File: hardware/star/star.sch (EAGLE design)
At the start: 153 parts, among them IC1 MAX481CSA, IC2 LD117AS12TR, IC22 LD117AS12TR, IC3 74HCT08D, IC4 7404D, IC8 MAX481CSA, K1 T90-12VDC-TL-A, K2 T90-12VDC-TL-A, K5 AQG22110, K6 AQG22110, P1 B3B-PH-K, Q1 35A/25V/8.5mΩ, Q2 35A/25V/8.5mΩ, Q3 35A/25V/8.5mΩ, Q4 35A/25V/8.5mΩ, T1 T_PNP_MMBT5401_CHANGJ_SOT23-B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, T2 T_PNP_MMBT5401_CHANGJ_SOT23-B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, T3 T_PNP_MMBT5401_CHANGJ_SOT23-B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, T4 T_PNP_MMBT5401_CHANGJ_SOT23-B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, U1 TCLT1600, X1 MKDSN1,5/2-5,08, X2 MKDSN1,5/2-5,08, X3 MKDSN1,5/5-5,08

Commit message: I think it's good?
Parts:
- removed FIRE: MKDSN1,5/8-5,08, con-phoenix-508-jm:MKDSN1,5/8-5,08
- removed P1: B3B-PH-K, con-jst-ph:B3B-PH-K
- removed TVS1, TVS2, TVS3, TVS4: (no value), diode:DIODE-DO214AA
- removed X1, X2: MKDSN1,5/2-5,08, con-phoenix-508-jm:MKDSN1,5/2-5,08
- removed X3: MKDSN1,5/5-5,08, con-phoenix-508-jm:MKDSN1,5/5-5,08
- added 12VAC_IN, 5V/2_IN: MKDSN1,5/2-5,08, con-phoenix-508-jm:MKDSN1,5/2-5,08
- added D10, D11, D139, D20, D21, D5: SMBJ8.0CA, SMBJ8.0CA:SMBJ8.0CA
- added D22, D23, D24, D25, D26, D27, D28, D29, D30, D31: D_B5819W-SL_CHANGJ_SOD123, JLC PCB Basic Parts_loc:D_B5819W-SL_CHANGJ_SOD123
- added DMX_OUT, OVERRIDE_EN: B3B-PH-K, con-jst-ph:B3B-PH-K
- added FIRE_OUT: MKDSN1,5/8-5,08, con-phoenix-508-jm:MKDSN1,5/8-5,08
- added FOG_IN: MKDSN1,5/5-5,08, con-phoenix-508-jm:MKDSN1,5/5-5,08
- added K3: T90-12VDC-TL-A, relay:JT1A-PCB-DC12V
- added OVERRIDE_EN2: (no value), pinhead:PINHD-1X3
- added R50: R_1K_0603, JLC PCB Basic Parts_loc:R_1K_0603
- added R6: R_100K_0603, JLC PCB Basic Parts_loc:R_100K_0603
- D4: value (none) -> SMBJ8.0CA; device diode:DIODE-DO214AA -> SMBJ8.0CA:SMBJ8.0CA; DESCRIPTION (none) -> 600 Watt TVS 5.0v working, 9v clamp; LCSC_PART C80339 -> C78757
- LED_ARRAY: value (none) -> B4B-PH-K; device pinhead:PINHD-1X4 -> con-jst-ph:B4B-PH-K
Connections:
- new net N$53: FIRE_OUT-1.KL, K3G$2.P
- new net N$58: OVERRIDE_EN.1, OVERRIDE_EN2.1, R50.2
- net +14V: now also FIRE_OUT-3.KL; no longer FIRE-3.KL
- net +3V3: now also D22.C, D24.C, D26.C, D28.C, D30.C, R50.1
- net +5V: now also D15.C, D16.A, K3G$1.1
- net +5V/2: now also 5V/2_IN-2.KL, K3G$2.S; no longer D15.C, D16.A, FIRE-1.KL, X2-2.KL
- net 120_LINE: now also 12VAC_IN-1.KL; no longer X1-1.KL
- net 120_NEUTRAL: now also 12VAC_IN-2.KL, FIRE_OUT-6.KL, FIRE_OUT-8.KL, FOG_IN-5.KL; no longer FIRE-6.KL, FIRE-8.KL, X1-2.KL, X3-5.KL
- net 18: now also D21.2
- net 19: now also D4.2
- net BOOMER_BLOWER: now also D10.2
- net BOOMER_FUEL: now also D5.2
- net BOOMER_IGNITER: now also D11.2
- net GND: now also D10.1, D11.1, D139.1, D20.1, D21.1, D23.A, D25.A, D27.A, D29.A, D31.A, D4.1, D5.1, DMX_OUT.1, OVERRIDE_EN.3, OVERRIDE_EN2.3, Q4.S, R6.1; no longer D4.A, P1.1, TVS1.A, TVS2.A, TVS3.A, TVS4.A, X2-1.KL
- net GND3: now also 5V/2_IN-1.KL, FIRE_OUT-2.KL; no longer Q4.S
- net N$13: now also FOG_IN-2.KL; no longer X3-2.KL
- net N$14: now also FOG_IN-4.KL; no longer X3-4.KL
- net N$15: now also FOG_IN-1.KL; no longer X3-1.KL
- net N$17: now also D22.A, D23.C; no longer TVS1.C
- net N$22: now also OVERRIDE_EN.2, OVERRIDE_EN2.2
- net N$23: now also D30.A, D31.C, R6.2; no longer D4.C
- net N$25: now also D28.A, D29.C; no longer TVS4.C
- net N$31: now also D24.A, D25.C; no longer TVS2.C
- net N$37: now also D26.A, D27.C; no longer TVS3.C
- net N$48: now also FIRE_OUT-7.KL; no longer FIRE-7.KL
- net N$5: now also DMX_OUT.2; no longer P1.2
- net N$50: now also FIRE_OUT-5.KL; no longer FIRE-5.KL
- net N$51: now also FIRE_OUT-4.KL; no longer FIRE-4.KL
- net N$52: now also K3G$1.2; no longer FIRE-2.KL
- net N$6: now also DMX_OUT.3; no longer P1.3
- net N$7: now also FOG_IN-3.KL; no longer X3-3.KL
- net POOFER: now also D139.2
- net STAR_ENABLE: now also D20.2
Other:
- note removed: "Todo: Drive Q4 with +5 and GND Add Relay to switch +5/2 and GND3"
- moved on the sheet: 5V_CTRL_LAZERS, C1, C10, C11, C12, C13, C14, C15, C16, C17, C18, C19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

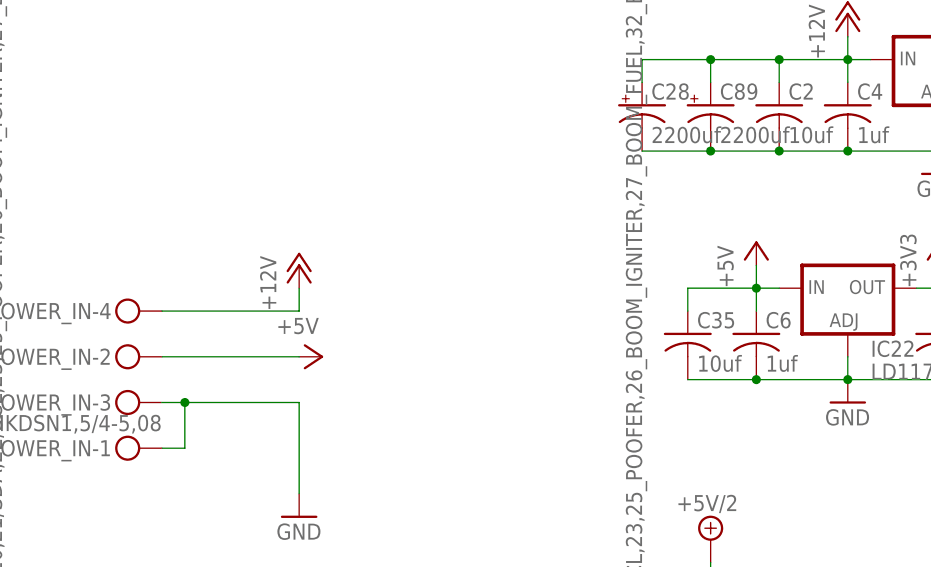
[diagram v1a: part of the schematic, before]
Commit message: Manual Routing Complete for v2
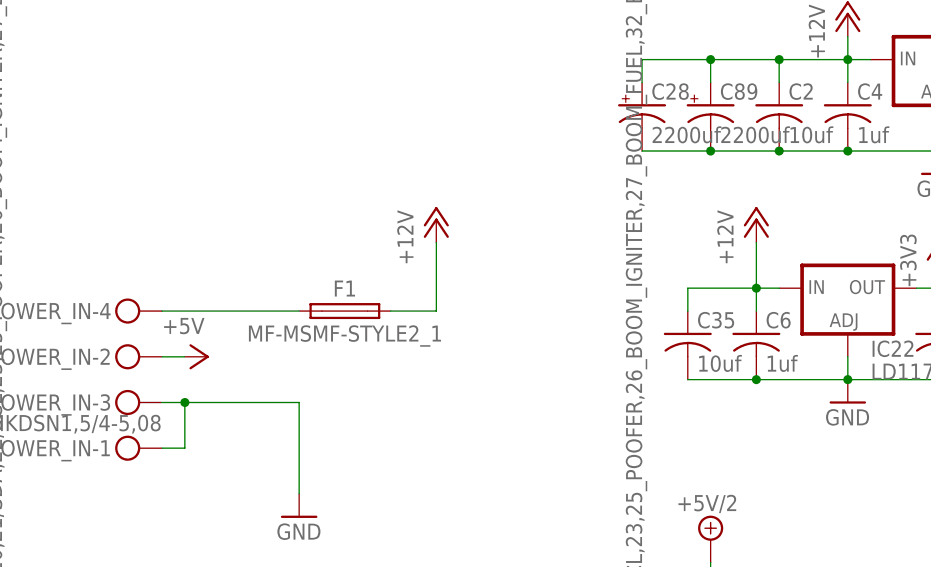
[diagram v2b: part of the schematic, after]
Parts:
- added F1: MF-MSMF-STYLE2_1, Fuse:MF-MSMF-STYLE2_1
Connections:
- new net N$59: F1.1, POWER_IN-4.KL
- net +12V: now also C35.1, C6.1, F1.2, IC22.IN; no longer POWER_IN-4.KL
- net +5V: no longer C35.1, C6.1, IC22.IN
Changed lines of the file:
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@@
 <attribute name="PRICE" value="0.5"/>
 </part>
-<part name="P+13" library="supply1" library_urn="urn:adsk.eagle:library:371" deviceset="+5V" device=""/>
 <part name="GND101" library="supply1" library_urn="urn:adsk.eagle:library:371" deviceset="GND" device=""/>
 <part name="C6" library="rcl" library_urn="urn:adsk.eagle:library:334" deviceset="C-US" device="C0805" package3d_urn="urn:adsk.eagle:package:23617/2" value="1uf">
@@
 <part name="+3V13" library="supply1" library_urn="urn:adsk.eagle:library:371" deviceset="+3V3" device=""/>
 <part name="OVERRIDE_EN2" library="pinhead" library_urn="urn:adsk.eagle:library:325" deviceset="PINHD-1X3" device="" package3d_urn="urn:adsk.eagle:package:22458/2"/>
+<part name="F1" library="Fuse" library_urn="urn:adsk.eagle:library:24934274" deviceset="MF-MSMF" device="-STYLE2_1" package3d_urn="urn:adsk.eagle:package:24934283/1">
+<attribute name="LCSC_PART" value="C78695"/>
+</part>
+<part name="P+10" library="supply1" library_urn="urn:adsk.eagle:library:371" deviceset="+12V" device=""/>
 </parts>
 <sheets>
@@
 <attribute name="VALUE" x="189.992" y="406.4762" size="1.778" layer="96"/>
 </instance>
-<instance part="P+5" gate="1" x="299.72" y="434.34" smashed="yes">
-<attribute name="VALUE" x="297.18" y="429.26" size="1.778" layer="96" rot="R90"/>
+<instance part="P+5" gate="1" x="314.96" y="439.42" smashed="yes">
+<attribute name="VALUE" x="312.42" y="434.34" size="1.778" layer="96" rot="R90"/>
 </instance>
-<instance part="P+6" gate="1" x="302.26" y="424.18" smashed="yes" rot="R270">
-<attribute name="VALUE" x="297.18" y="426.72" size="1.778" layer="96"/>
+<instance part="P+6" gate="1" x="289.56" y="424.18" smashed="yes" rot="R270">
+<attribute name="VALUE" x="284.48" y="426.72" size="1.778" layer="96"/>
 </instance>
 <instance part="GND10" gate="1" x="299.72" y="406.4" smashed="yes">
@@
 <attribute name="LCSC_PART" x="360.68" y="431.8" size="1.778" layer="96" display="off"/>
 </instance>
-<instance part="P+13" gate="1" x="350.52" y="436.88" smashed="yes">
-<attribute name="VALUE" x="347.98" y="431.8" size="1.778" layer="96" rot="R90"/>
-</instance>
 <instance part="GND101" gate="1" x="360.68" y="419.1" smashed="yes">
 <attribute name="VALUE" x="358.14" y="416.56" size="1.778" layer="96"/>
@@
 <attribute name="VALUE" x="379.73" y="259.08" size="1.778" layer="96"/>
 </instance>
+<instance part="F1" gate="G$1" x="304.8" y="429.26" smashed="yes">
+<attribute name="NAME" x="304.8" y="431.76" size="1.778" layer="95" align="center"/>
+<attribute name="VALUE" x="304.8" y="426.76" size="1.778" layer="96" align="center"/>
+<attribute name="LCSC_PART" x="304.8" y="429.26" size="1.778" layer="96" display="off"/>
+</instance>
+<instance part="P+10" gate="1" x="350.52" y="439.42" smashed="yes">
+<attribute name="VALUE" x="347.98" y="434.34" size="1.778" layer="96" rot="R90"/>
+</instance>
 </instances>
 <busses>
@@
 <net name="+12V" class="2">
 <segment>
-<pinref part="P+5" gate="1" pin="+12V"/>
-<wire x1="299.72" y1="431.8" x2="299.72" y2="429.26" width="0.1524" layer="91"/>
-<wire x1="299.72" y1="429.26" x2="284.48" y2="429.26" width="0.1524" layer="91"/>
-<pinref part="POWER_IN" gate="-4" pin="KL"/>
-</segment>
-<segment>
 <pinref part="P+12" gate="1" pin="+12V"/>
 <wire x1="302.26" y1="172.72" x2="302.26" y2="190.5" width="0.1524" layer="91"/>
@@
 <junction x="378.46" y="396.24"/>
 </segment>
+<segment>
+<pinref part="F1" gate="G$1" pin="2"/>
+<pinref part="P+5" gate="1" pin="+12V"/>
+<wire x1="309.88" y1="429.26" x2="314.96" y2="429.26" width="0.1524" layer="91"/>
+<wire x1="314.96" y1="429.26" x2="314.96" y2="436.88" width="0.1524" layer="91"/>
+</segment>
+<segment>
+<pinref part="IC22" gate="G$1" pin="IN"/>
+<wire x1="350.52" y1="431.8" x2="353.06" y2="431.8" width="0.1524" layer="91"/>
+<pinref part="C35" gate="G$1" pin="1"/>
+<wire x1="350.52" y1="431.8" x2="342.9" y2="431.8" width="0.1524" layer="91"/>
+<wire x1="342.9" y1="431.8" x2="342.9" y2="429.26" width="0.1524" layer="91"/>
+<junction x="350.52" y="431.8"/>
+<pinref part="C6" gate="G$1" pin="1"/>
+<wire x1="350.52" y1="431.8" x2="350.52" y2="429.26" width="0.1524" layer="91"/>
+<pinref part="P+10" gate="1" pin="+12V"/>
+<wire x1="350.52" y1="431.8" x2="350.52" y2="436.88" width="0.1524" layer="91"/>
+</segment>
 </net>
 <net name="+5V" class="3">
@@
 <pinref part="P+6" gate="1" pin="+5V"/>
 <pinref part="POWER_IN" gate="-2" pin="KL"/>
-<wire x1="284.48" y1="424.18" x2="299.72" y2="424.18" width="0.1524" layer="91"/>
+<wire x1="284.48" y1="424.18" x2="287.02" y2="424.18" width="0.1524" layer="91"/>
 </segment>
 <segment>
@@
 </segment>
 <segment>
-<pinref part="P+13" gate="1" pin="+5V"/>
-<pinref part="IC22" gate="G$1" pin="IN"/>
-<wire x1="350.52" y1="434.34" x2="350.52" y2="431.8" width="0.1524" layer="91"/>
-<wire x1="350.52" y1="431.8" x2="353.06" y2="431.8" width="0.1524" layer="91"/>
-<pinref part="C35" gate="G$1" pin="1"/>
-<wire x1="350.52" y1="431.8" x2="342.9" y2="431.8" width="0.1524" layer="91"/>
-<wire x1="342.9" y1="431.8" x2="342.9" y2="429.26" width="0.1524" layer="91"/>
-<junction x="350.52" y="431.8"/>
-<pinref part="C6" gate="G$1" pin="1"/>
-<wire x1="350.52" y1="431.8" x2="350.52" y2="429.26" width="0.1524" layer="91"/>
-</segment>
-<segment>
 <pinref part="P+24" gate="1" pin="+5V"/>
 <wire x1="248.92" y1="259.08" x2="248.92" y2="254" width="0.1524" layer="91"/>
@@
 </segment>
 </net>
+<net name="N$59" class="0">
+<segment>
+<pinref part="POWER_IN" gate="-4" pin="KL"/>
+<pinref part="F1" gate="G$1" pin="1"/>
+<wire x1="284.48" y1="429.26" x2="299.72" y2="429.26" width="0.1524" layer="91"/>
+</segment>
+</net>

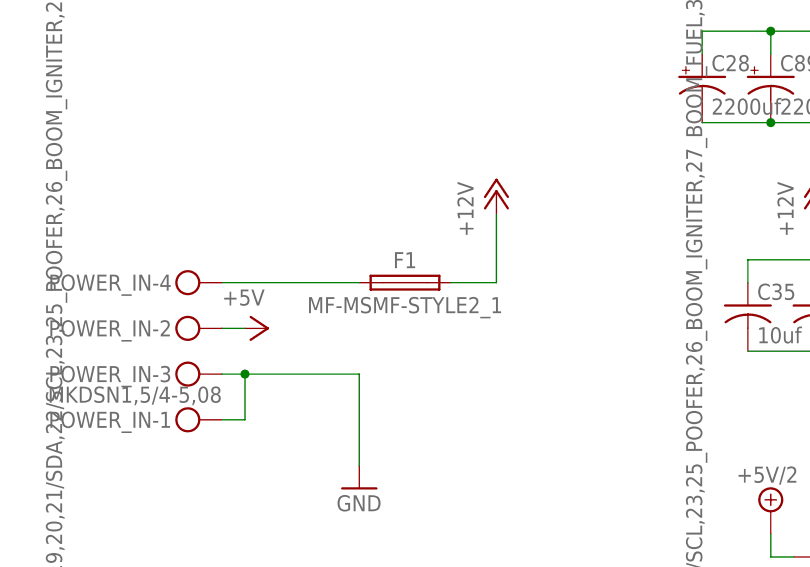
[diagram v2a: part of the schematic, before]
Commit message: Swapped 1.5A fuse with 5A fuse
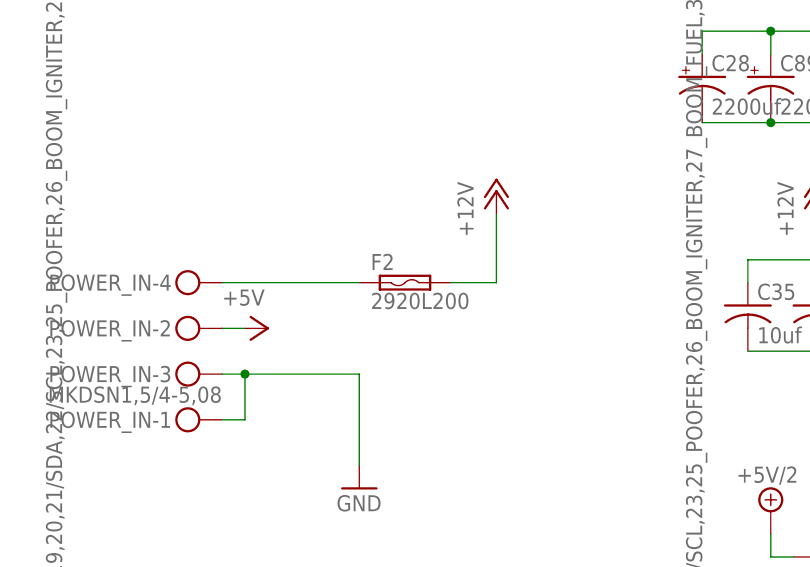
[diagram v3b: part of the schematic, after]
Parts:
- removed F1: MF-MSMF-STYLE2_1, Fuse:MF-MSMF-STYLE2_1
- added F2: 2920L200, 2920L200:2920L200
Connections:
- net +12V: now also F2.2; no longer F1.2
- net N$59: now also F2.1; no longer F1.1
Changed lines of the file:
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@@
 <part name="+3V13" library="supply1" library_urn="urn:adsk.eagle:library:371" deviceset="+3V3" device=""/>
 <part name="OVERRIDE_EN2" library="pinhead" library_urn="urn:adsk.eagle:library:325" deviceset="PINHD-1X3" device="" package3d_urn="urn:adsk.eagle:package:22458/2"/>
-<part name="F1" library="Fuse" library_urn="urn:adsk.eagle:library:24934274" deviceset="MF-MSMF" device="-STYLE2_1" package3d_urn="urn:adsk.eagle:package:24934283/1">
-<attribute name="LCSC_PART" value="C78695"/>
-</part>
 <part name="P+10" library="supply1" library_urn="urn:adsk.eagle:library:371" deviceset="+12V" device=""/>
+<part name="F2" library="2920L200" library_urn="urn:adsk.eagle:library:39262743" deviceset="2920L200" device="" package3d_urn="urn:adsk.eagle:package:39262746/1">
+<attribute name="LCSC_PART" value="C910846"/>
+<attribute name="MF" value=""/>
+</part>
 </parts>
 <sheets>
@@
 <attribute name="VALUE" x="379.73" y="259.08" size="1.778" layer="96"/>
 </instance>
-<instance part="F1" gate="G$1" x="304.8" y="429.26" smashed="yes">
-<attribute name="NAME" x="304.8" y="431.76" size="1.778" layer="95" align="center"/>
-<attribute name="VALUE" x="304.8" y="426.76" size="1.778" layer="96" align="center"/>
-<attribute name="LCSC_PART" x="304.8" y="429.26" size="1.778" layer="96" display="off"/>
-</instance>
 <instance part="P+10" gate="1" x="350.52" y="439.42" smashed="yes">
 <attribute name="VALUE" x="347.98" y="434.34" size="1.778" layer="96" rot="R90"/>
 </instance>
+<instance part="F2" gate="G$1" x="304.8" y="429.26" smashed="yes">
+<attribute name="NAME" x="300.98456875" y="430.658990625" size="1.780540625" layer="95"/>
+<attribute name="VALUE" x="300.98786875" y="426.33736875" size="1.778990625" layer="96"/>
+<attribute name="LCSC_PART" x="304.8" y="429.26" size="1.778" layer="96" display="off"/>
+</instance>
 </instances>
 <busses>
@@
 </segment>
 <segment>
-<pinref part="F1" gate="G$1" pin="2"/>
 <pinref part="P+5" gate="1" pin="+12V"/>
 <wire x1="309.88" y1="429.26" x2="314.96" y2="429.26" width="0.1524" layer="91"/>
 <wire x1="314.96" y1="429.26" x2="314.96" y2="436.88" width="0.1524" layer="91"/>
+<pinref part="F2" gate="G$1" pin="2"/>
 </segment>
 <segment>
@@
 <segment>
 <pinref part="POWER_IN" gate="-4" pin="KL"/>
-<pinref part="F1" gate="G$1" pin="1"/>
 <wire x1="284.48" y1="429.26" x2="299.72" y2="429.26" width="0.1524" layer="91"/>
+<pinref part="F2" gate="G$1" pin="1"/>
 </segment>
 </net>

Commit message: Updated labels
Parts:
- renumbered I2C_2 to I2C
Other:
- note added: "Device Enable"
- note added: "Microcontroller"
- moved on the sheet: C17, D10, D11, D139, D15, D30, D31, D5, FIRE_OUT-6, IC4A, IC4B, IC4C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
